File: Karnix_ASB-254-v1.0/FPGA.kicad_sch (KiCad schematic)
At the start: 48 parts, among them U5 LFE5U-25F-BG256C, U7 W25Q128JVPIQ, Y2 25 MHz

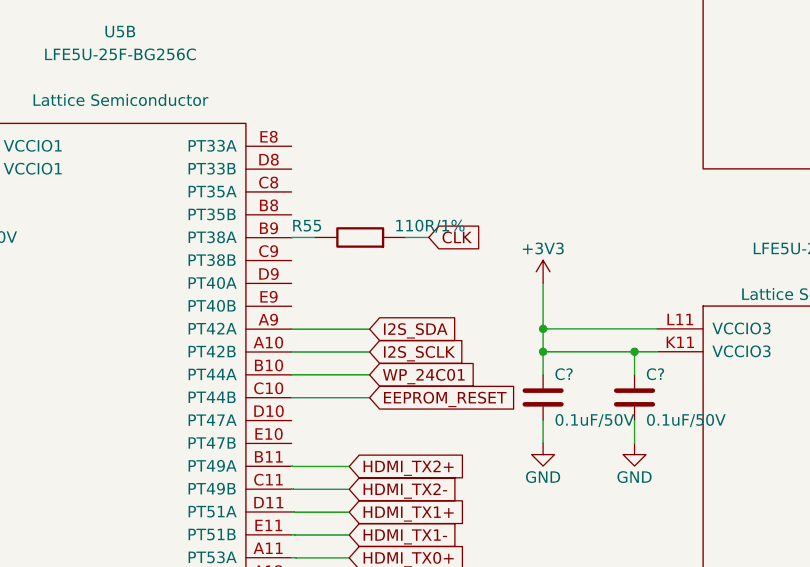
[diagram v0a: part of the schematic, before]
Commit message: Rework HDMI wiring: - Connect SDL, SCL and CEC signals to FPGA through level converters - Separate HDMI power rails with diodes
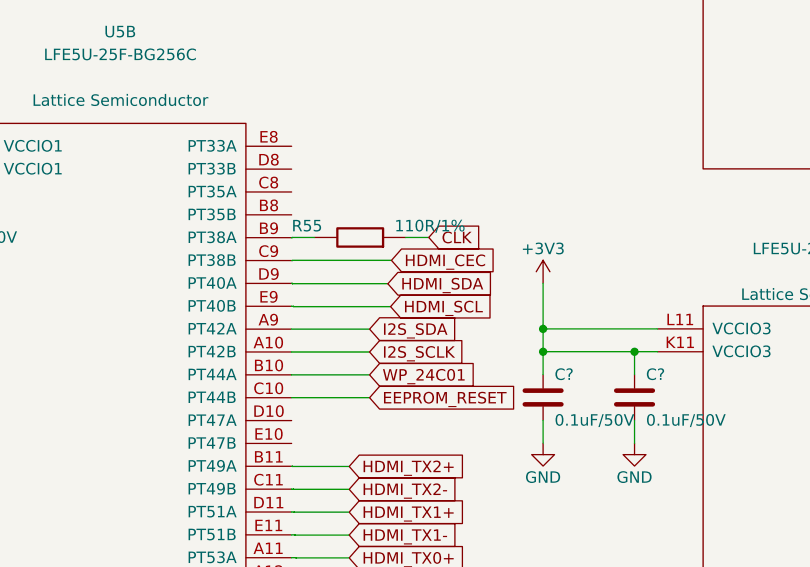
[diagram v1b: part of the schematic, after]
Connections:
- net HDMI_CEC: now reaches U5.C9 (PT38B)
- net HDMI_SDA: now reaches U5.D9 (PT40A)
- net HDMI_SCL: now reaches U5.E9 (PT40B)
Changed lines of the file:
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@@
+    (stroke (width 0) (type default))
+  )
+  (wire (pts (xy 89.2 125.1) (xy 78.2 125.1))
     (stroke (width 0) (type default))
   )
@@
     (stroke (width 0) (type default))
   )
+  (wire (pts (xy 78.2 125.1204) (xy 78.105 125.1204))
+    (stroke (width 0) (type default))
+  )
   (wire (pts (xy 382.905 142.875) (xy 382.905 145.415))
     (stroke (width 0) (type default))
@@
     (stroke (width 0) (type default))
   )
+  (wire (pts (xy 78.2 127.6604) (xy 78.105 127.6604))
+    (stroke (width 0) (type default))
+  )
   (wire (pts (xy 161.925 48.895) (xy 156.845 48.895))
     (stroke (width 0) (type default))
@@
     (stroke (width 0) (type default))
   )
+  (wire (pts (xy 78.3 130.2004) (xy 78.105 130.2004))
+    (stroke (width 0) (type default))
+  )
   (wire (pts (xy 342.265 201.295) (xy 339.725 201.295))
     (stroke (width 0) (type default))
@@
     (stroke (width 0) (type default))
   )
+  (wire (pts (xy 78.2 127.7) (xy 78.2 127.6604))
+    (stroke (width 0) (type default))
+  )
   (wire (pts (xy 235.585 170.815) (xy 250.825 170.815))
     (stroke (width 0) (type default))
@@
     (stroke (width 0) (type default))
   )
+  (wire (pts (xy 78.3 130.24) (xy 78.3 130.2004))
+    (stroke (width 0) (type default))
+  )
   (wire (pts (xy 382.905 198.755) (xy 380.365 198.755))
     (stroke (width 0) (type default))
@@
     (stroke (width 0) (type default))
   )
+  (wire (pts (xy 78.2 125.1) (xy 78.2 125.1204))
+    (stroke (width 0) (type default))
+  )
   (wire (pts (xy 161.925 170.815) (xy 156.845 170.815))
     (stroke (width 0) (type default))
@@
     (stroke (width 0) (type default))
   )
+  (wire (pts (xy 89.1 130.24) (xy 78.3 130.24))
+    (stroke (width 0) (type default))
+  )
   (wire (pts (xy 78.613 168.3004) (xy 78.105 168.3004))
     (stroke (width 0) (type default))
@@
   )
   (wire (pts (xy 78.359 181.0004) (xy 78.105 181.0004))
+    (stroke (width 0) (type default))
+  )
+  (wire (pts (xy 88.8 127.7) (xy 78.2 127.7))
     (stroke (width 0) (type default))
   )
@@
     )
   )
+  (global_label "HDMI_CEC" (shape input) (at 89.2 125.1 0) (fields_autoplaced)
+    (effects (font (size 1.27 1.27)) (justify left))
+    (property "Intersheetrefs" "${INTERSHEET_REFS}" (at 98.0049 125.1 0)
+      (effects (font (size 1.27 1.27)) (justify left) hide)
+    )
+  )
   (global_label "RS485_DE" (shape input) (at 93.472 89.535 0)
     (effects (font (size 1.27 1.27)) (justify left))
@@
     )
   )
+  (global_label "HDMI_SDA" (shape input) (at 88.8 127.7 0) (fields_autoplaced)
+    (effects (font (size 1.27 1.27)) (justify left))
+    (property "Intersheetrefs" "${INTERSHEET_REFS}" (at 98.0913 127.7 0)
+      (effects (font (size 1.27 1.27)) (justify left) hide)
+    )
+  )
   (global_label "JTAG_TDO" (shape input) (at 271.145 97.155 180)
     (effects (font (size 1.27 1.27)) (justify right))
@@
     )
   )
+  (global_label "HDMI_SCL" (shape input) (at 89.1 130.24 0) (fields_autoplaced)
+    (effects (font (size 1.27 1.27)) (justify left))
+    (property "Intersheetrefs" "${INTERSHEET_REFS}" (at 98.0265 130.24 0)
+      (effects (font (size 1.27 1.27)) (justify left) hide)
+    )
+  )

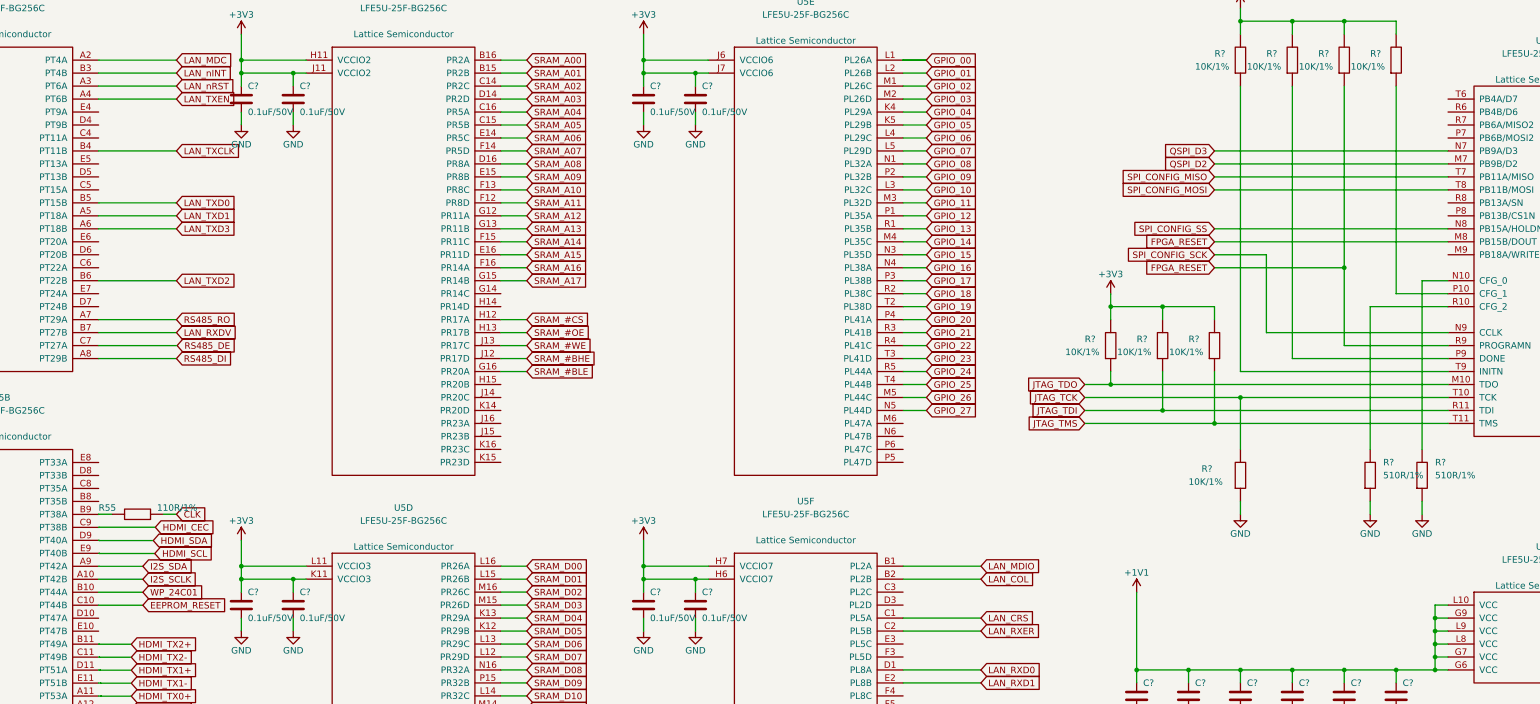
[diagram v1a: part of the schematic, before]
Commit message: Route HDMI and its environment
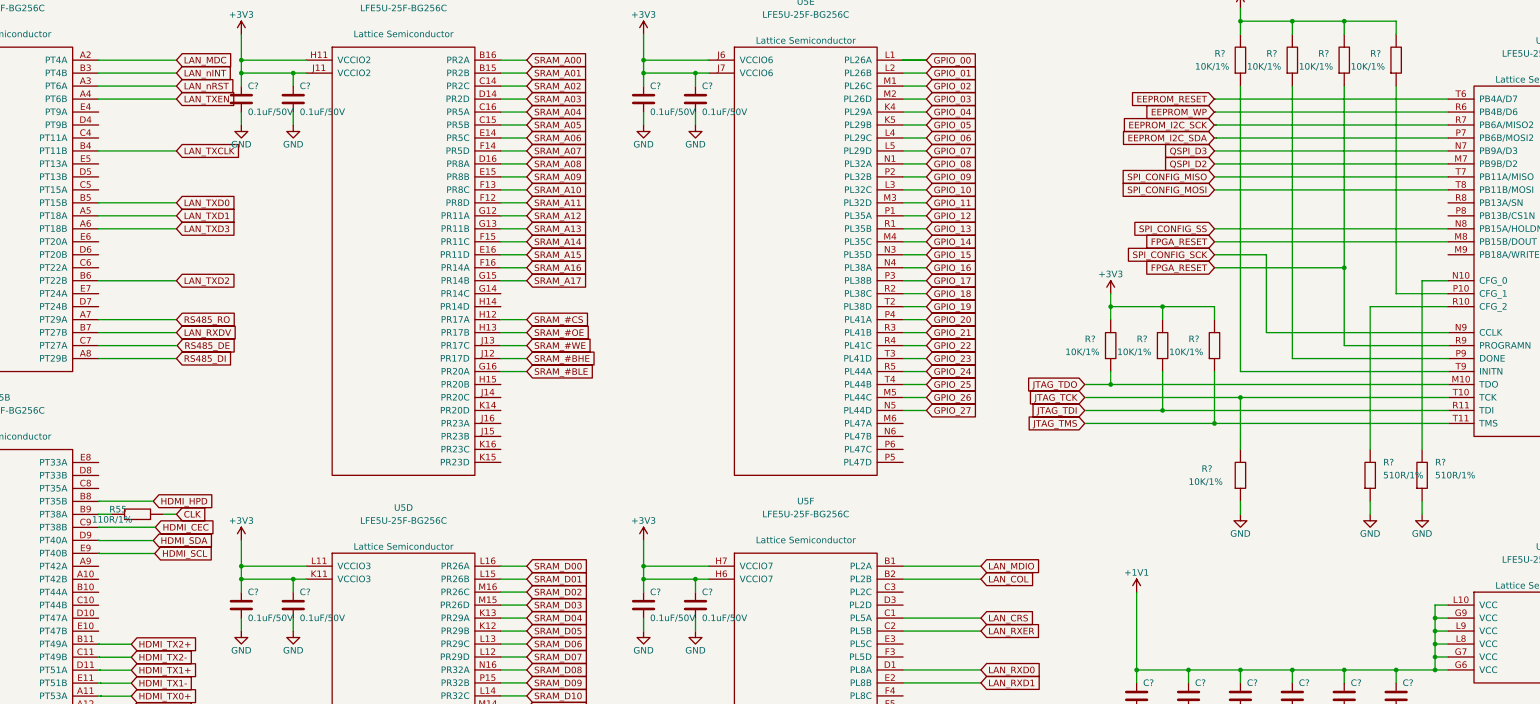
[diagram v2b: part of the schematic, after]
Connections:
- net EEPROM_RESET: now also U5.T6 (PB4A/D7); no longer U5.C10 (PT44B)
- net HDMI_HPD: now reaches U5.B8 (PT35B)
- net EEPROM_I2C_SDA: now reaches U5.P7 (PB6B/MOSI2)
- net EEPROM_WP: now reaches U5.R6 (PB4B/D6)
- net EEPROM_I2C_SCK: now reaches U5.R7 (PB6A/MISO2)
- net I2S_SCLK: no longer names the net of U5.A10 (PT42B)
- net I2S_SDA: no longer names the net of U5.A9 (PT42A)
- net WP_24C01: no longer names the net of U5.B10 (PT44A)
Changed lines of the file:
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@@
     (stroke (width 0) (type default))
   )
+  (wire (pts (xy 88.8 120) (xy 78.2 120))
+    (stroke (width 0) (type default))
+  )
   (wire (pts (xy 271.145 104.775) (xy 296.545 104.775))
     (stroke (width 0) (type default))
@@
     (stroke (width 0) (type default))
   )
+  (wire (pts (xy 296.9 48.9) (xy 296.9 48.895))
+    (stroke (width 0) (type default))
+  )
   (wire (pts (xy 339.725 208.915) (xy 339.725 219.075))
     (stroke (width 0) (type default))
@@
     (stroke (width 0) (type default))
   )
-  (wire (pts (xy 86.7664 137.8204) (xy 78.105 137.8204))
+  (wire (pts (xy 296.7 43.82) (xy 296.7 43.815))
     (stroke (width 0) (type default))
   )
@@
     (stroke (width 0) (type default))
   )
-  (wire (pts (xy 86.7664 132.7404) (xy 78.105 132.7404))
-    (stroke (width 0) (type default))
-  )
   (wire (pts (xy 301.625 153.035) (xy 291.465 153.035))
     (stroke (width 0) (type default))
@@
     (stroke (width 0) (type default))
   )
+  (wire (pts (xy 296.7 43.815) (xy 342.265 43.815))
+    (stroke (width 0) (type default))
+  )
   (wire (pts (xy 321.945 26.035) (xy 332.105 26.035))
     (stroke (width 0) (type default))
@@
     (stroke (width 0) (type default))
   )
+  (wire (pts (xy 296.5 46.36) (xy 296.8 46.36))
+    (stroke (width 0) (type default))
+  )
   (wire (pts (xy 116.205 135.255) (xy 106.045 135.255))
     (stroke (width 0) (type default))
@@
     (stroke (width 0) (type default))
   )
+  (wire (pts (xy 296.6 41.28) (xy 296.6 41.275))
+    (stroke (width 0) (type default))
+  )
   (wire (pts (xy 380.365 208.915) (xy 382.905 208.915))
     (stroke (width 0) (type default))
@@
     (stroke (width 0) (type default))
   )
+  (wire (pts (xy 296.8 46.355) (xy 342.265 46.355))
+    (stroke (width 0) (type default))
+  )
   (wire (pts (xy 240.157 74.295) (xy 235.585 74.295))
     (stroke (width 0) (type default))
@@
     (stroke (width 0) (type default))
   )
+  (wire (pts (xy 296.6 41.275) (xy 342.265 41.275))
+    (stroke (width 0) (type default))
+  )
   (wire (pts (xy 84.5 153.08) (xy 78.4 153.08))
     (stroke (width 0) (type default))
@@
     (stroke (width 0) (type default))
   )
+  (wire (pts (xy 296.5 43.82) (xy 296.7 43.82))
+    (stroke (width 0) (type default))
+  )
   (wire (pts (xy 234.9 208.94) (xy 234.9 208.915))
     (stroke (width 0) (type default))
@@
     (stroke (width 0) (type default))
   )
+  (wire (pts (xy 78.2 120) (xy 78.2 120.0404))
+    (stroke (width 0) (type default))
+  )
   (wire (pts (xy 339.725 178.435) (xy 339.725 180.975))
     (stroke (width 0) (type default))
@@
     (stroke (width 0) (type default))
   )
+  (wire (pts (xy 78.2 120.0404) (xy 78.105 120.0404))
+    (stroke (width 0) (type default))
+  )
   (wire (pts (xy 136.525 269.875) (xy 121.285 269.875))
     (stroke (width 0) (type default))
@@
     (stroke (width 0) (type default))
   )
-  (wire (pts (xy 86.7664 135.2804) (xy 78.105 135.2804))
-    (stroke (width 0) (type default))
-  )
   (wire (pts (xy 342.265 206.375) (xy 339.725 206.375))
     (stroke (width 0) (type default))
@@
     (stroke (width 0) (type default))
   )
+  (wire (pts (xy 296.8 46.36) (xy 296.8 46.355))
+    (stroke (width 0) (type default))
+  )
   (wire (pts (xy 342.265 145.415) (xy 339.725 145.415))
     (stroke (width 0) (type default))
@@
     (stroke (width 0) (type default))
   )
+  (wire (pts (xy 296.9 48.895) (xy 342.265 48.895))
+    (stroke (width 0) (type default))
+  )
   (wire (pts (xy 339.725 188.595) (xy 339.725 191.135))
     (stroke (width 0) (type default))
@@
     (stroke (width 0) (type default))
   )
+  (wire (pts (xy 296.5 41.28) (xy 296.6 41.28))
+    (stroke (width 0) (type default))
+  )
   (wire (pts (xy 37.465 36.195) (xy 37.465 38.735))
     (stroke (width 0) (type default))
@@
     (stroke (width 0) (type default))
   )
+  (wire (pts (xy 296.5 48.9) (xy 296.9 48.9))
+    (stroke (width 0) (type default))
+  )
   (wire (pts (xy 380.365 206.375) (xy 382.905 206.375))
     (stroke (width 0) (type default))
@@
     (stroke (width 0) (type default))
   )
-  (wire (pts (xy 86.7664 140.3604) (xy 78.105 140.3604))
-    (stroke (width 0) (type default))
-  )
   (wire (pts (xy 78.2574 175.9204) (xy 78.2574 175.895))
     (stroke (width 0) (type default))
@@
     )
   )
-  (global_label "WP_24C01" (shape input) (at 86.7664 137.8204 0)
-    (effects (font (size 1.27 1.27)) (justify left))
-    (property "Intersheetrefs" "${INTERSHEET_REFS}" (at 86.7664 137.8204 0)
-      (effects (font (size 1.27 1.27)) hide)
-    )
-  )
   (global_label "HDMI_TX1-" (shape input) (at 84.5 155.62 0) (fields_autoplaced)
     (effects (font (size 1.27 1.27)) (justify left))
@@
     )
   )
-  (global_label "I2S_SCLK" (shape input) (at 86.7664 135.2804 0)
-    (effects (font (size 1.27 1.27)) (justify left))
-    (property "Intersheetrefs" "${INTERSHEET_REFS}" (at 86.7664 135.2804 0)
-      (effects (font (size 1.27 1.27)) hide)
-    )
-  )
   (global_label "GPIO_14" (shape input) (at 240.157 69.215 0)
     (effects (font (size 1.27 1.27)) (justify left))
@@
     )
   )
+  (global_label "EEPROM_WP" (shape input) (at 296.5 43.82 180)
+    (effects (font (size 1.27 1.27)) (justify right))
+    (property "Intersheetrefs" "${INTERSHEET_REFS}" (at 296.5 43.82 0)
+      (effects (font (size 1.27 1.27)) hide)
+    )
+  )
   (global_label "HDMI_CEC" (shape input) (at 89.2 125.1 0) (fields_autoplaced)
     (effects (font (size 1.27 1.27)) (justify left))
@@
     )
   )
-  (global_label "I2S_SDA" (shape input) (at 86.7664 132.7404 0)
-    (effects (font (size 1.27 1.27)) (justify left))
-    (property "Intersheetrefs" "${INTERSHEET_REFS}" (at 86.7664 132.7404 0)
-      (effects (font (size 1.27 1.27)) hide)
-    )
-  )
   (global_label "LAN_CRS" (shape input) (at 250.825 142.875 0)
     (effects (font (size 1.27 1.27)) (justify left))
@@
     )
   )
-  (global_label "EEPROM_RESET" (shape input) (at 86.7664 140.3604 0)
-    (effects (font (size 1.27 1.27)) (justify left))
-    (property "Intersheetrefs" "${INTERSHEET_REFS}" (at 86.7664 140.3604 0)
-      (effects (font (size 1.27 1.27)) hide)
-    )
-  )
   (global_label "LAN_nRST" (shape input) (at 93.345 38.735 0)
     (effects (font (size 1.27 1.27)) (justify left))
@@
     )
   )
+  (global_label "HDMI_HPD" (shape input) (at 88.8 120 0) (fields_autoplaced)
+    (effects (font (size 1.27 1.27)) (justify left))
+    (property "Intersheetrefs" "${INTERSHEET_REFS}" (at 97.9697 120 0)
+      (effects (font (size 1.27 1.27)) (justify left) hide)
+    )
+  )
   (global_label "ADC_SPI_CSn" (shape input) (at 247.6 203.86 0) (fields_autoplaced)
     (effects (font (size 1.27 1.27)) (justify left))
@@
     )
   )
+  (global_label "EEPROM_I2C_SDA" (shape input) (at 296.5 48.9 180)
+    (effects (font (size 1.27 1.27)) (justify right))
+    (property "Intersheetrefs" "${INTERSHEET_REFS}" (at 296.5 48.9 0)
+      (effects (font (size 1.27 1.27)) hide)
+    )
+  )
   (global_label "LAN_TXEN" (shape input) (at 93.345 41.275 0)
     (effects (font (size 1.27 1.27)) (justify left))
@@
     )
   )
+  (global_label "EEPROM_RESET" (shape input) (at 296.5 41.28 180)
+    (effects (font (size 1.27 1.27)) (justify right))
+    (property "Intersheetrefs" "${INTERSHEET_REFS}" (at 296.5 41.28 0)
+      (effects (font (size 1.27 1.27)) hide)
+    )
+  )
   (global_label "GPIO_22" (shape input) (at 240.157 89.535 0)
     (effects (font (size 1.27 1.27)) (justify left))
@@
     )
   )
+  (global_label "EEPROM_I2C_SCK" (shape input) (at 296.5 46.36 180)
+    (effects (font (size 1.27 1.27)) (justify right))
+    (property "Intersheetrefs" "${INTERSHEET_REFS}" (at 296.5 46.36 0)
+      (effects (font (size 1.27 1.27)) hide)
+    )
+  )
   (global_label "SRAM_#OE" (shape input) (at 161.925 86.995 0)
     (effects (font (size 1.27 1.27)) (justify left))
@@
   (symbol (lib_id "Fabmicro:Resistor") (at 85.725 122.555 0) (unit 1)
     (in_bom yes) (on_board yes) (dnp no)
-    (property "Reference" "R55" (at 78.105 121.285 0)
+    (property "Reference" "R55" (at 80.2 121.6 0)
       (effects (font (size 1.27 1.27)) (justify left))
     )
-    (property "Value" "110R/1%" (at 89.535 121.285 0)
+    (property "Value" "110R/1%" (at 76.8 123.6 0)
       (effects (font (size 1.27 1.27)) (justify left))
     )
